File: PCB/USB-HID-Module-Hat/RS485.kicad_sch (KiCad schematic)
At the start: 21 parts, among them J1 Raspberry_Pi_2_3, J2 RJHSE-5381, U1 MAX3535ECWI+T

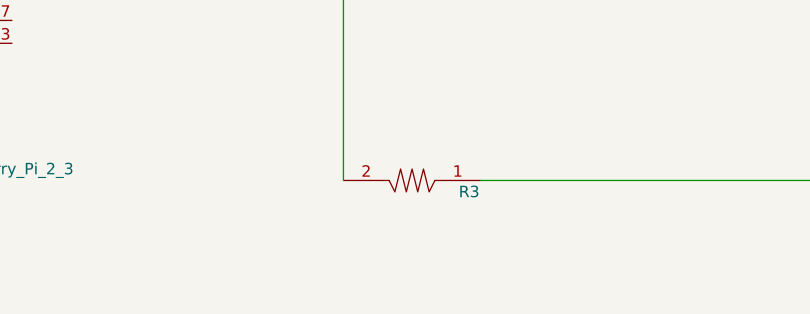
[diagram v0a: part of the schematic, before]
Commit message: PCB
PCB layout 80% complete. Board shape defined. Components and connectors places !
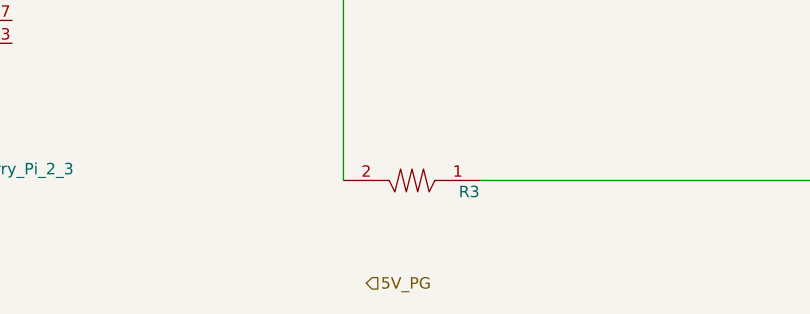
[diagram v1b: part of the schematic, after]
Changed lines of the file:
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@@
+		)
+	)
+	(hierarchical_label "5V_PG"
+		(shape input)
+		(at 129.54 151.13 0)
+		(fields_autoplaced yes)
+		(effects
+			(font
+				(size 1.27 1.27)
+			)
+			(justify left)
 		)
 	)
